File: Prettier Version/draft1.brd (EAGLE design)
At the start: 160 x 100 mm, 12 parts, among them J2 CONN-51P-FPC-MOLEX, J4 DISPLAYPORT-SINK-MOLEX

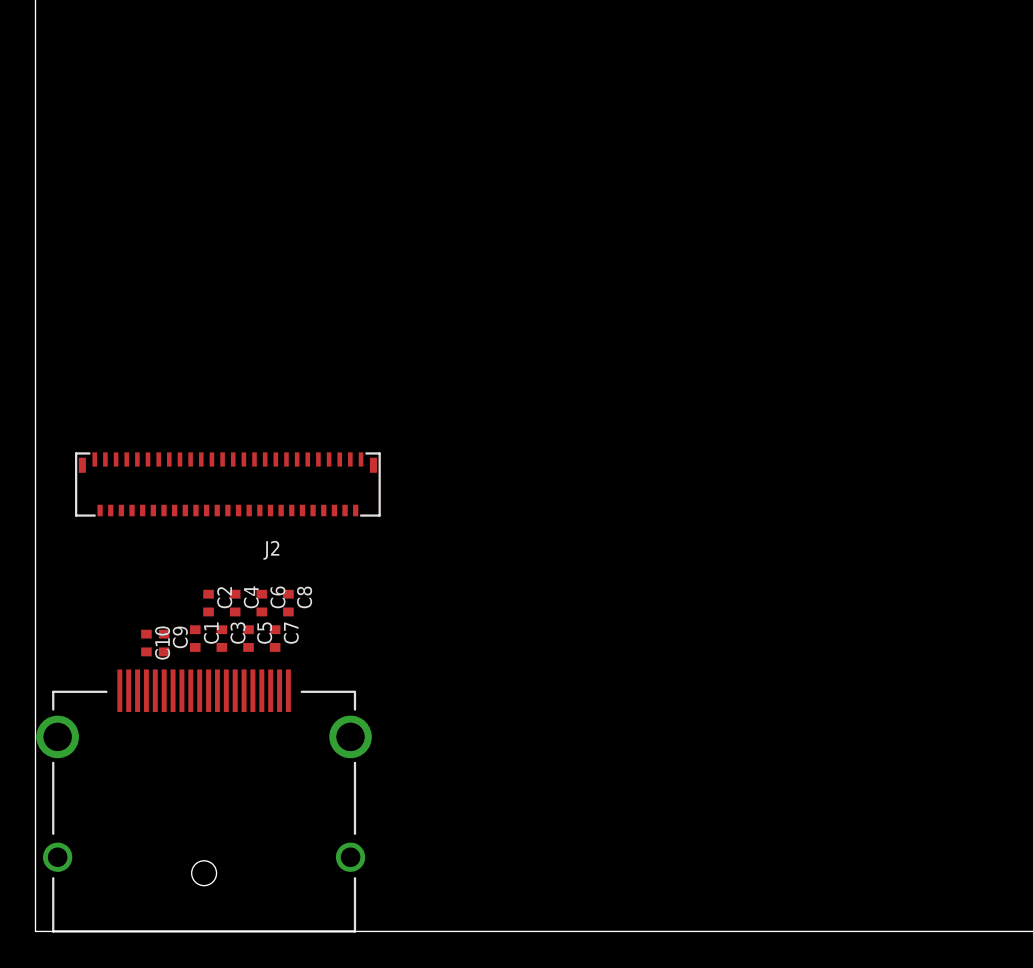
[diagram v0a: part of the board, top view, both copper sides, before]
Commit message: Schematic work
Added LED control
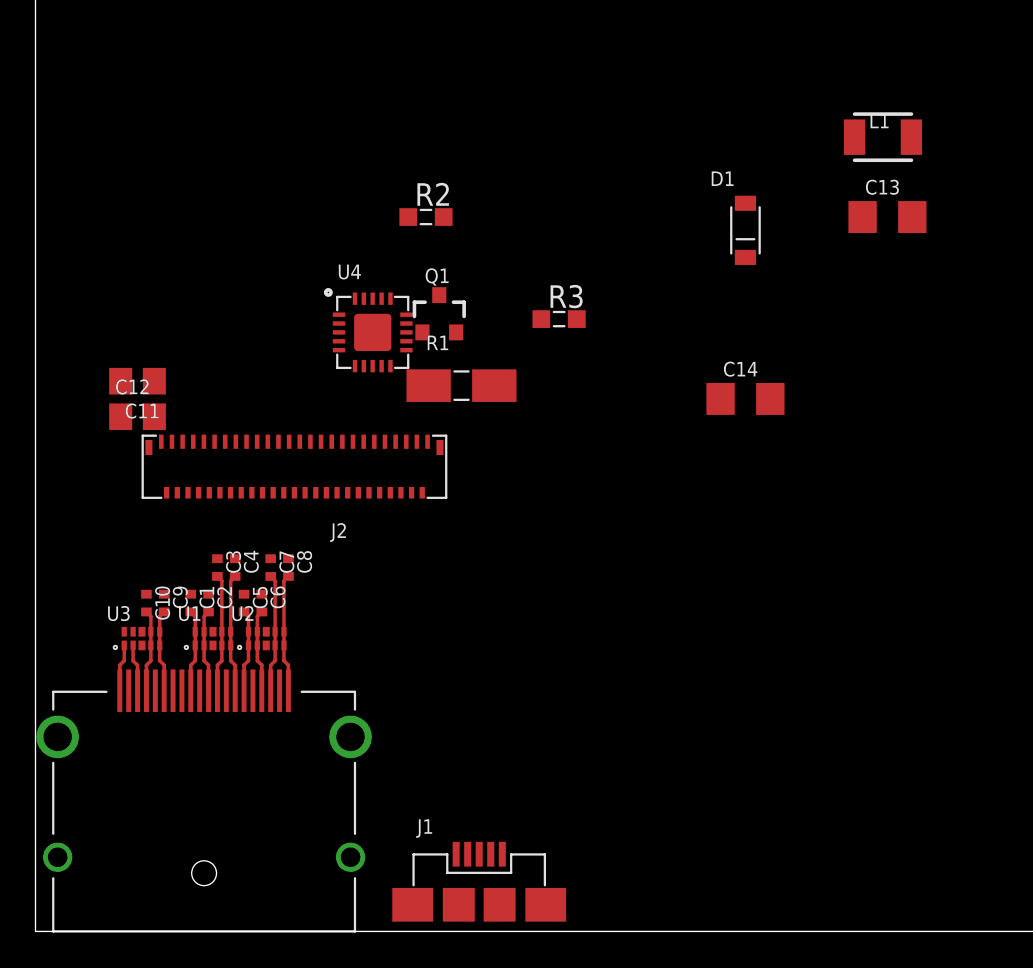
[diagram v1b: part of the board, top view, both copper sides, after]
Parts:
- added C11: 100n, 00-EvaLibrary:C0805
- added C12: 1u, 00-EvaLibrary:C0805
- added C13: 10u, 00-EvaLibrary:C1206
- added C14: 2.2u, 00-EvaLibrary:C1206
- added D1: DB2W40300L, 00-EvaLibrary:MINI2-F3-B
- added J1: USB_MICRO_AB, 00-EvaLibrary:USB_MICRO_AB
- added L1: 2.2u, 00-EvaLibrary:1210
- added Q1: Si2304, SparkFun-DiscreteSemi:SOT23-3
- added R1: 50m, 00-EvaLibrary:MCS1632
- added R2: 1M, 00-EvaLibrary:R0603
- added R3: 43.2K, 00-EvaLibrary:R0603
- added U1, U2, U3: ESD-SUPPRESSOR-4-TPD4S010-DQA, 00-EvaLibrary:SON-10
- added U4: MAX8790A-TQFN-20, 00-EvaLibrary:TQFN-20
- moved C3 4.01 mm to (10.2, 20.5)
- moved C7 4.01 mm to (13.2, 20.5)
- moved J2 3.88 mm to (14.6, 28.0)
- moved C10 2.25 mm to (6.25, 18.5)
- moved C9 2.25 mm to (7.25, 18.5)
- moved C1 2.02 mm to (8.75, 18.5)
- moved C5 2.02 mm to (11.8, 18.5)
- moved C4 2.00 mm to (11.2, 20.5)
- moved C8 2.00 mm to (14.2, 20.5)
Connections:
- removed net LED_A1A: J2.48
- removed net LED_A1B: J2.49
- removed net LED_A2A: J2.45
- removed net LED_A2B: J2.46
- new net LED_A1: C14.1, D1.1, J2.48, J2.49, R2.2
- new net LED_A2: J2.45, J2.46
- new net N$11: Q1.2, R1.2, U4.12
- new net N$12: C13.1, J1.1, L1.1, U4.1, U4.15, U4.16, U4.18, U4.4
- new net N$13: Q1.1, U4.13
- new net N$14: D1.2, L1.2, Q1.3
- new net N$15: R2.1, R3.2, U4.14
- net 3.3V: now also C11.1, C12.1, U3.1
- net GND: now also C11.2, C12.2, C13.2, C14.2, J1.5, J1.GND1, J1.GND2, J1.GND3, J1.GND4, R1.1, R3.1, U1.3, U1.8, U2.3, U2.8, U3.3, U3.8, U4.8, U4.PAD
- net HPD: now also U3.2
- net LED_K1A: now also U4.11
- net LED_K2A: now also U4.10
- net LED_K3A: now also U4.9
- net LED_K4A: now also U4.7
- net LED_K5A: now also U4.6
- net LED_K6A: now also U4.5
- net N$1: now also C4.2, J4.7, U1.5; no longer C1.2, J4.12
- net N$10: now also U3.4
- net N$2: now also C3.2, J4.9, U1.4; no longer C2.2, J4.10
- net N$3: now also C2.2, J4.10, U1.2; no longer C3.2, J4.9
- net N$4: now also C1.2, J4.12, U1.1; no longer C4.2, J4.7
- net N$5: now also U2.1
- net N$6: now also U2.2
- net N$7: now also U2.4
- net N$8: now also U2.5
- net N$9: now also U3.5
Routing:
- net N$8: track 0.00 -> 6.65 mm
- net N$7: track 0.00 -> 6.65 mm
- net N$2: track 0.00 -> 6.65 mm
- net N$1: track 0.00 -> 6.65 mm
- net N$9: track 0.00 -> 4.65 mm
- net N$6: track 0.00 -> 4.65 mm
- net N$5: track 0.00 -> 4.65 mm
- net N$4: track 0.00 -> 4.65 mm
- net N$3: track 0.00 -> 4.65 mm
- net N$10: track 0.00 -> 4.65 mm
- net HPD: track 0.00 -> 2.66 mm
- net 3.3V: track 0.00 -> 2.66 mm

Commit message: Prelim. PCB layout
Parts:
- removed J1: USB_MICRO_AB, 00-EvaLibrary:USB_MICRO_AB
- removed J4: DISPLAYPORT-SINK-MOLEX, 00-EvaLibrary:MOLEX-47272-0028
- added C15, C18: 0.1u, 00-EvaLibrary:C0603
- added C16, C19, C20, C21: 1u, 00-EvaLibrary:C0603
- added C17: 2.2u, 00-EvaLibrary:C1206
- added D2: DB2W40300L, 00-EvaLibrary:MINI2-F3-B
- added DP: DISPLAYPORT-SINK-MOLEX, 00-EvaLibrary:MOLEX-47272-0028
- added ISP: AVR_SPI_PRG_6PTH, SparkFun-Connectors:2X3
- added L2: 2.2u, 00-EvaLibrary:1210
- added Q2: Si2304, SparkFun-DiscreteSemi:SOT23-3
- added R10, R9: 22, 00-EvaLibrary:R0603
- added R11, R12: 4.7K, 00-EvaLibrary:R0603
- added R4, R8: 1.2K, 00-EvaLibrary:R0603
- added R5: 50m, 00-EvaLibrary:MCS1632
- added R6: 1M, 00-EvaLibrary:R0603
- added R7: 43.2K, 00-EvaLibrary:R0603
- added SERIAL: HEADER-6X1-961106-5500, 00-EvaLibrary:HEADER-3M-961-6P-2.54MM
- added TOUCH: HEADER-6X1-FPC-LOWER_CONTACT, 00-EvaLibrary:SFV6R-1STE1HLF
- added U5: MAX8790A-TQFN-20, 00-EvaLibrary:TQFN-20
- added U6: ATMEGA32U4-QFN-44, 00-EvaLibrary:QFN-44
- added U7: TLV700DDC, 00-EvaLibrary:SOT-23-5
- added USB: USB_MICRO_AB, 00-EvaLibrary:USB_MICRO_AB
- moved C13 52.1 mm to (7.50, 7.50), turned to 90 degrees
- moved C3 40.3 mm to (50.5, 21.2)
- moved C4 40.3 mm to (51.5, 21.2)
- moved C7 40.3 mm to (53.5, 21.2)
- moved C8 40.3 mm to (54.5, 21.2)
- moved C1 40.3 mm to (49.0, 19.0)
- moved C10 40.3 mm to (46.5, 19.0)
- moved C2 40.3 mm to (50.0, 19.0)
- moved C5 40.3 mm to (52.0, 19.0)
- moved C6 40.3 mm to (53.0, 19.0)
- moved C9 40.3 mm to (47.5, 19.0)
- moved U1 40.3 mm to (50.2, 17.0)
- moved U2 40.3 mm to (53.2, 17.0)
- moved U3 40.3 mm to (46.2, 17.0)
- moved C12 39.3 mm to (43.8, 19.0), turned to 180 degrees
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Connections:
- new net !RESET: ISP.5, U6.13
- new net BRIGHTNESS1: U4.3
- new net BRIGHTNESS2: U5.3
- new net CTS: SERIAL.5, U6.22
- new net D+: R9.2, USB.3
- new net D-: R10.2, USB.2
- new net D3.3V: C21.1, R11.2, R12.2, TOUCH.5, U6.14, U6.24, U6.34, U6.44, U7.5
- new net INT: TOUCH.4, U6.32
- new net MISO: ISP.1, U6.11
- new net MOSI: ISP.4, U6.10
- new net N$16: R4.2, U4.17
- new net N$17: C15.1, R4.1
- new net N$18: D2.2, L2.2, Q2.3
- new net N$19: Q2.2, R5.2, U5.12
- new net N$20: R6.1, R7.2, U5.14
- new net N$21: R8.2, U5.17
- new net N$22: C18.1, R8.1
- new net N$23: R9.1, U6.4
- new net N$24: R10.1, U6.3
- new net N$25: C20.1, U6.6
- new net RTS: SERIAL.1, U6.12
- new net RXD: SERIAL.3, U6.20
- new net SCL: R11.1, TOUCH.3, U6.18
- new net SCLK: ISP.3, U6.9
- new net SCREEN_!RESET: TOUCH.1, U6.37
- new net SDA: R12.1, TOUCH.2, U6.19
- new net TXD: SERIAL.2, U6.21
- new net VBUS: C13.1, C16.1, C19.1, ISP.2, L1.1, L2.1, SERIAL.4, U4.1, U4.15, U4.16, U4.18, U4.19, U4.4, U5.1, U5.15, U5.16, U5.18, U5.19, U5.4, U6.2, U6.7, U7.1, U7.3, USB.1
- net 3.3V: now also DP.20; no longer J4.20
- net GND: now also C15.2, C16.2, C17.2, C18.2, C19.2, C20.2, C21.2, DP.11, DP.16, DP.19, DP.2, DP.5, DP.8, DP.GND1, DP.GND2, DP.GND3, DP.GND4, ISP.6, R5.1, R7.1, SERIAL.6, TOUCH.6, U4.2, U5.2, U5.8, U5.PAD, U6.15, U6.23, U6.35, U6.43, U6.5, U6.PAD, U7.2, USB.5, USB.GND1, USB.GND2, USB.GND3, USB.GND4; no longer J1.5, J1.GND1, J1.GND2, J1.GND3, J1.GND4, J4.11, J4.16, J4.19, J4.2, J4.5, J4.8, J4.GND1, J4.GND2, J4.GND3, J4.GND4
- net HPD: now also DP.18; no longer J4.18
- net LED_A2: now also C17.1, D2.1, R6.2
- net LED_K1B: now also U5.11
- net LED_K2B: now also U5.7
- net LED_K3A: now also U4.6; no longer U4.9
- net LED_K3B: now also U5.10
- net LED_K4A: now also U4.9; no longer U4.7
- net LED_K4B: now also U5.6
- net LED_K5A: now also U4.5; no longer U4.6
- net LED_K5B: now also U5.9
- net LED_K6A: now also U4.7; no longer U4.5
- net LED_K6B: now also U5.5
- net N$1: now also DP.7; no longer J4.7
- net N$10: now also DP.17; no longer J4.17
- net N$12: now also Q2.1, U5.13; no longer C13.1, J1.1, L1.1, U4.1, U4.15, U4.16, U4.18, U4.4
- net N$2: now also DP.9; no longer J4.9
- net N$3: now also DP.10; no longer J4.10
- net N$4: now also DP.12; no longer J4.12
- net N$5: now also DP.6; no longer J4.6
- net N$6: now also DP.4; no longer J4.4
- net N$7: now also DP.3; no longer J4.3
- net N$8: now also DP.1; no longer J4.1
- net N$9: now also DP.15; no longer J4.15
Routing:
- net GND: track 0.00 -> 74.4 mm, vias 0 -> 43
- net VBUS: track 0.00 -> 65.0 mm, vias 0 -> 7
- net LED_A1: track 0.00 -> 57.1 mm, vias 0 -> 2
- net LED_A2: track 0.00 -> 56.4 mm, vias 0 -> 2
- net LED_K1B: track 0.00 -> 52.6 mm
- net LED_K3B: track 0.00 -> 49.1 mm
- net LED_K5B: track 0.00 -> 46.2 mm
- net LED_K2B: track 0.00 -> 43.2 mm, vias 0 -> 2
- net LED_K4B: track 0.00 -> 39.5 mm, vias 0 -> 2
- net LED_K6B: track 0.00 -> 35.7 mm, vias 0 -> 2
- net LED_K1A: track 0.00 -> 33.3 mm, vias 0 -> 2
- net LED_K2A: track 0.00 -> 29.8 mm
- net LED_K4A: track 0.00 -> 28.0 mm
- net LED_K3A: track 0.00 -> 27.5 mm, vias 0 -> 2
- net LED_K5A: track 0.00 -> 25.2 mm, vias 0 -> 2
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- added copper zone on layer 1, net 3.3V
- added copper zone on layer 3, net D3.3V
- added copper zone on layer 1, net GND
- added copper zone on layer 2, net GND
- added copper zone on layer 3, net GND
- added copper zone on layer 3, net VBUS
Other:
- board size 160 x 100 mm -> 60 x 36 mm

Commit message: Misc updates
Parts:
- added C22, C23: 18p, 00-EvaLibrary:C0603
- added X1: 16MHz, 00-EvaLibrary:ABM3C
- moved R11 13.0 mm to (7.25, 21.2), turned to 90 degrees
- moved R12 10.3 mm to (7.25, 17.8)
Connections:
- new net N$26: C22.1, U6.16, X1.1
- new net N$27: C23.1, U6.17, X1.3
- net GND: now also C22.2, C23.2, X1.2, X1.4
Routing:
- net N$26: track 0.00 -> 8.92 mm
- net N$27: track 0.00 -> 7.55 mm
- net D3.3V: track 11.5 -> 8.87 mm, vias 7 -> 8
- net SCL: track 20.6 -> 18.3 mm
- net GND: track 74.4 -> 73.3 mm, vias 43 -> 44
- net !RESET: track 13.1 -> 12.5 mm

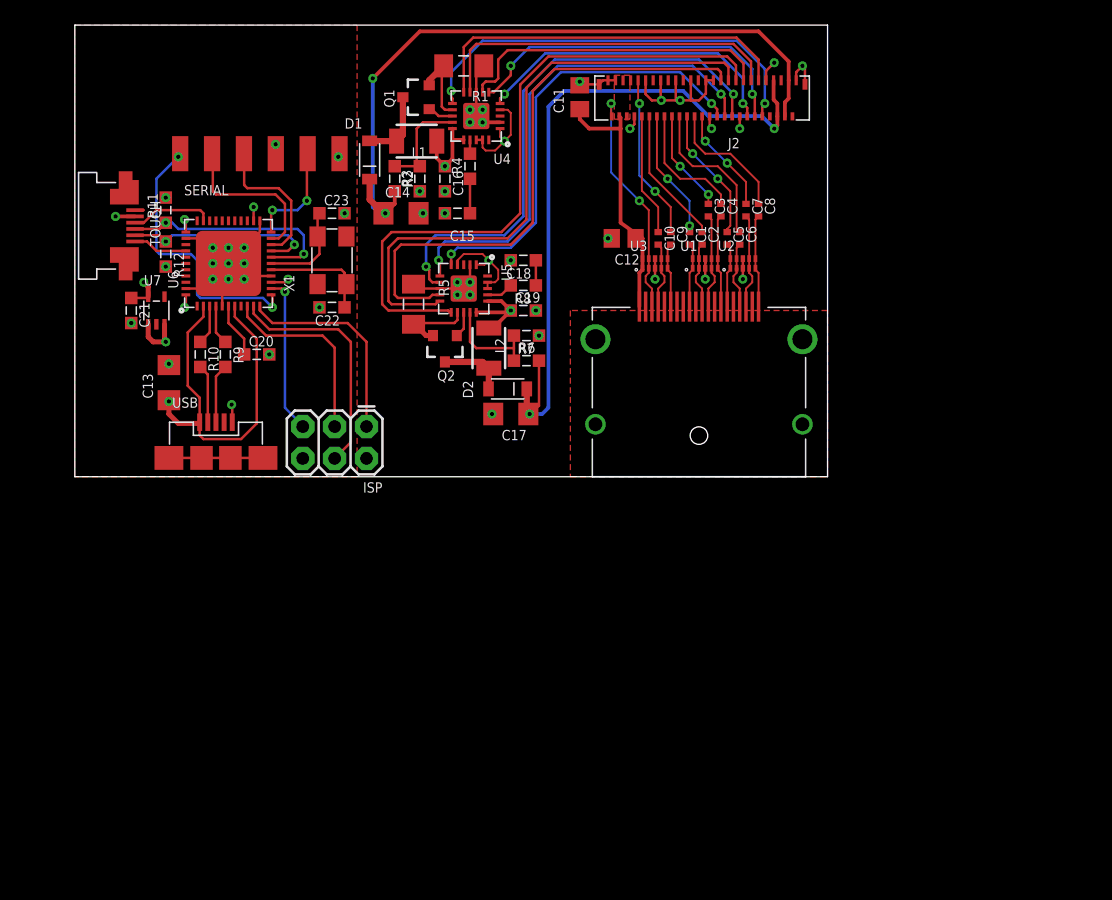
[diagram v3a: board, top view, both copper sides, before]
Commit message: Deleted PCB layout
Pending physical measurements
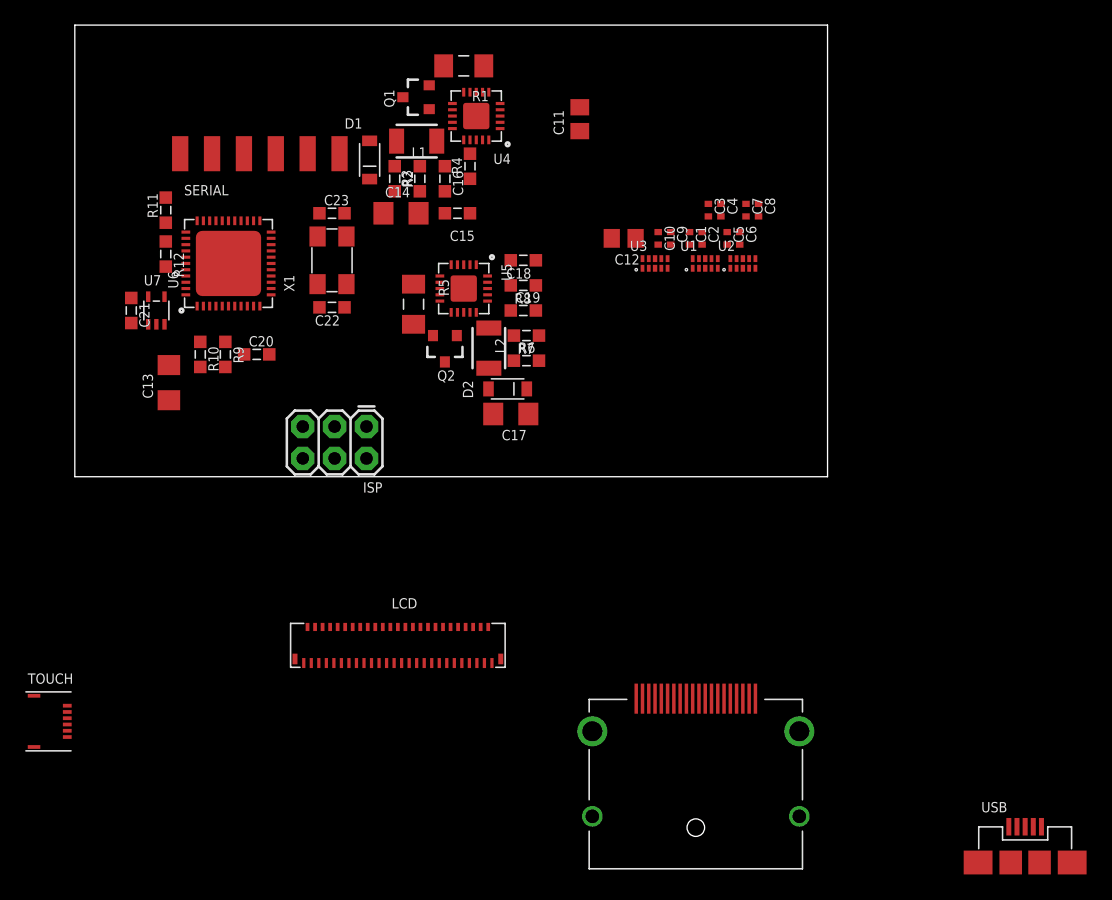
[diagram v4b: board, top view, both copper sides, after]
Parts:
- removed J2: CONN-51P-FPC-MOLEX, 00-EvaLibrary:MOLEX-502250-5191
- added LCD: CONN-51P-FPC-MOLEX, 00-EvaLibrary:MOLEX-502250-5191
- TOUCH: value HEADER-6X1-FPC-LOWER_CONTACT -> HEADER-6X1-FPC-DUAL_CONTACT; device 00-EvaLibrary:SFV6R-1STE1HLF -> 00-EvaLibrary:MOLEX-503480-0600
- moved USB 72.1 mm to (75.8, -30.8)
- moved TOUCH 40.4 mm to (-3.75, -19.5)
- moved DP 31.3 mm to (49.5, -31.2)
- moved C11 1.75 mm to (40.2, 28.5)
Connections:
- net 3.3V: now also LCD.4, LCD.5, LCD.6, LCD.7; no longer J2.4, J2.5, J2.6, J2.7
- net AUX_N: now also LCD.10; no longer J2.10
- net AUX_P: now also LCD.9; no longer J2.9
- net BRIGHTNESS1: now also U6.29
- net BRIGHTNESS2: now also U6.27
- net GND: now also LCD.1, LCD.11, LCD.15, LCD.19, LCD.23, LCD.27, LCD.28, LCD.29, LCD.3, LCD.36, LCD.43, LCD.51, LCD.8, LCD.GND1, LCD.GND2; no longer J2.1, J2.11, J2.15, J2.19, J2.23, J2.27, J2.28, J2.29, J2.3, J2.36, J2.43, J2.51, J2.8, J2.GND1, J2.GND2
- net HPD: now also LCD.2; no longer J2.2
- net LANE0_N: now also LCD.12; no longer J2.12
- net LANE0_P: now also LCD.14; no longer J2.14
- net LANE1_N: now also LCD.16; no longer J2.16
- net LANE1_P: now also LCD.18; no longer J2.18
- net LANE2_N: now also LCD.20; no longer J2.20
- net LANE2_P: now also LCD.22; no longer J2.22
- net LANE3_N: now also LCD.24; no longer J2.24
- net LANE3_P: now also LCD.26; no longer J2.26
- net LED_A1: now also LCD.48, LCD.49; no longer J2.48, J2.49
- net LED_A2: now also LCD.45, LCD.46; no longer J2.45, J2.46
- net LED_K1A: now also LCD.42; no longer J2.42
- net LED_K1B: now also LCD.35; no longer J2.35
- net LED_K2A: now also LCD.41; no longer J2.41
- net LED_K2B: now also LCD.34; no longer J2.34
- net LED_K3A: now also LCD.40; no longer J2.40
- net LED_K3B: now also LCD.33; no longer J2.33
- net LED_K4A: now also LCD.39; no longer J2.39
- net LED_K4B: now also LCD.32; no longer J2.32
- net LED_K5A: now also LCD.38; no longer J2.38
- net LED_K5B: now also LCD.31; no longer J2.31
- net LED_K6A: now also LCD.37; no longer J2.37
- net LED_K6B: now also LCD.30; no longer J2.30
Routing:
- net GND: track 73.3 -> 0.00 mm, vias 44 -> 0
- net VBUS: track 65.0 -> 0.00 mm, vias 7 -> 0
- net LED_A1: track 57.1 -> 0.00 mm, vias 2 -> 0
- net LED_A2: track 56.4 -> 0.00 mm, vias 2 -> 0
- net LED_K1B: track 52.6 -> 0.00 mm
- net LED_K3B: track 49.1 -> 0.00 mm
- net LED_K5B: track 46.2 -> 0.00 mm
- net LED_K2B: track 43.2 -> 0.00 mm, vias 2 -> 0
- net LED_K4B: track 39.5 -> 0.00 mm, vias 2 -> 0
- net LED_K6B: track 35.7 -> 0.00 mm, vias 2 -> 0
- net LED_K1A: track 33.3 -> 0.00 mm, vias 2 -> 0
- net LED_K2A: track 29.8 -> 0.00 mm
- net LED_K4A: track 28.0 -> 0.00 mm
- net LED_K3A: track 27.5 -> 0.00 mm, vias 2 -> 0
- net LED_K5A: track 25.2 -> 0.00 mm, vias 2 -> 0
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- removed copper zone on layer 1, net 3.3V
- removed copper zone on layer 3, net D3.3V
- removed copper zone on layer 1, net GND
- removed copper zone on layer 2, net GND
- removed copper zone on layer 3, net GND
- removed copper zone on layer 3, net VBUS
